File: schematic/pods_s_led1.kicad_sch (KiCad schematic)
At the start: 4 parts, among them Q2 IRLZ44N

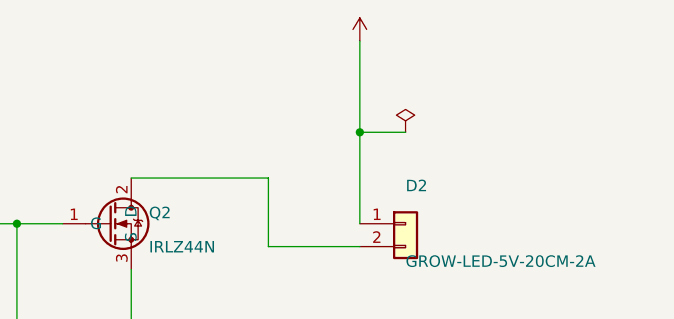
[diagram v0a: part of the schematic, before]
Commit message: Split PUMP_5V/LED_5V rails per SKiDL truth; flat draft guard
Pump/LED sheets used power:+5V symbols, joining the separately-fused
F2/F3 branches. Now PUMP_5V/LED_5V global labels; netlists match
pods.net pin-for-pin (full compare zero). pods.py flatness=1.0 so the
SKiDL draft can never clobber placed pods_s_* sheets. Docs net names.
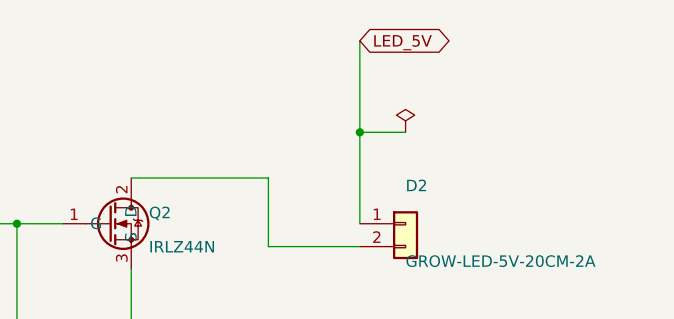
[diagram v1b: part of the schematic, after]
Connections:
- net +5V renamed LED_5V
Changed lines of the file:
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@@
   (junction (at 99.06 88.9) (diameter 0) (color 0 0 0 0)
 )
-  (symbol
-    (lib_id "power:+5V")
+  (global_label "LED_5V"
+    (shape bidirectional)
     (at 124.46 53.34 0)
-    (unit 1)
-    (exclude_from_sim no)
-    (in_bom no)
-    (on_board yes)
-    (dnp no)
-    (fields_autoplaced no)
-    (property "Reference" "#+5V04"
-      (at 124.46 53.34 0)
-      (effects (font (size 1.27 1.27)) (hide yes)))
-    (property "Value" "+5V"
-      (at 124.46 53.34 0)
-      (effects (font (size 1.27 1.27)) (hide yes)))
-    (pin "1"
+    (effects (font (size 1.27 1.27)) (justify left))
 )
-    (instances
-      (project "GrowMate"
-        (path "/216fdad8-4006-4d85-8157-93191bd90b6a/aa84ae83-c52b-5517-9ae5-9507ffaa1848"
-          (reference "#+5V04")
-          (unit 1)))))
   (wire
     (pts
@@
     (dnp no)
     (fields_autoplaced no)
-    (property "Reference" "#PWR05"
+    (property "Reference" "#PWR04"
       (at 129.54 63.5 0)
       (effects (font (size 1.27 1.27)) (hide yes)))
@@
       (project "GrowMate"
         (path "/216fdad8-4006-4d85-8157-93191bd90b6a/aa84ae83-c52b-5517-9ae5-9507ffaa1848"
-          (reference "#PWR05")
+          (reference "#PWR04")
           (unit 1)))))
   (wire
